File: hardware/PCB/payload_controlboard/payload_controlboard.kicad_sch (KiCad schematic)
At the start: 1 part

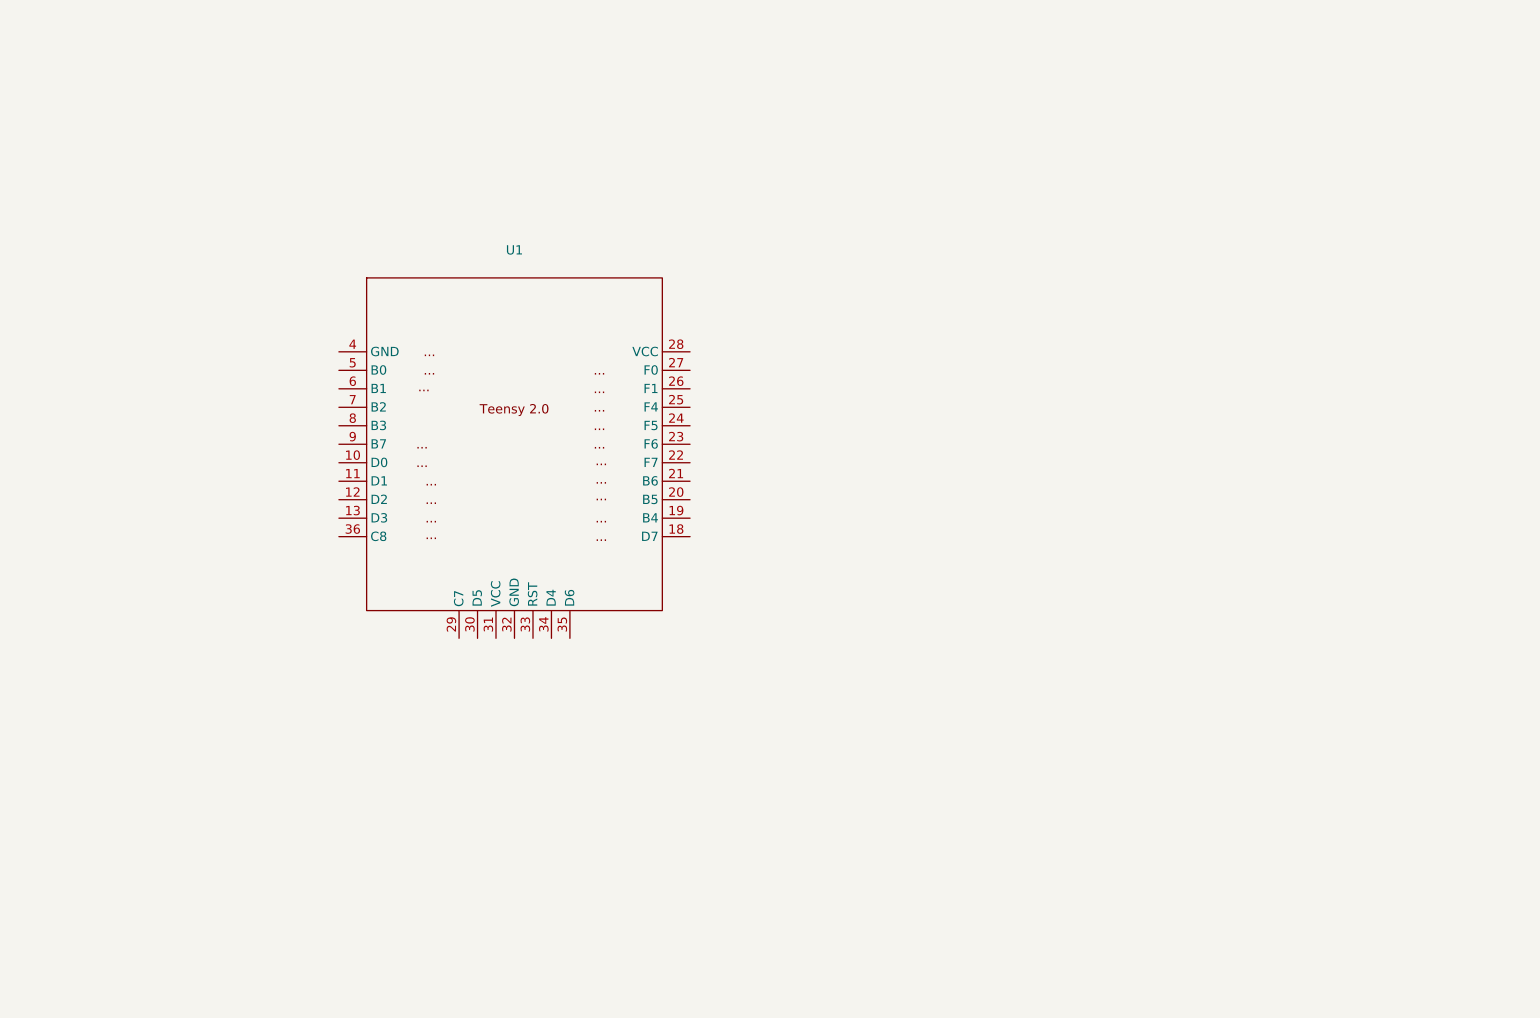
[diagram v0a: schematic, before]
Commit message: Initial payload control board and connector layout
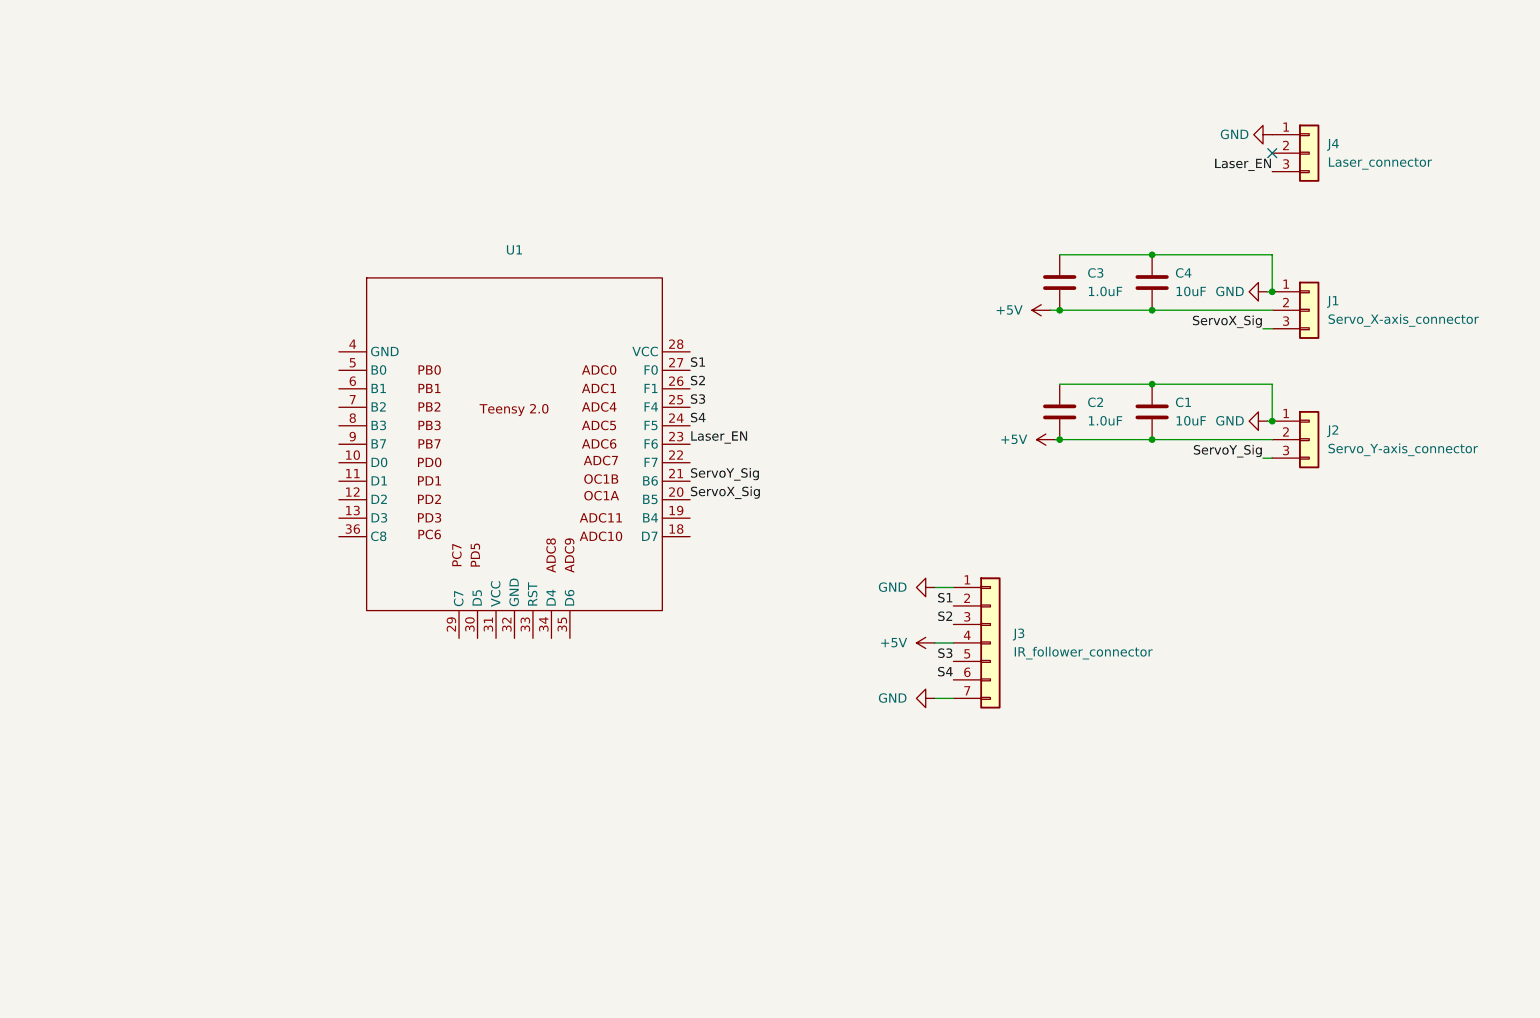
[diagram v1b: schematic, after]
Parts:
- added C1, C4: 10uF, symbol Device:C
- added C2, C3: 1.0uF, symbol Device:C
- added J1: Servo_X-axis_connector, symbol Connector_Generic:Conn_01x03
- added J2: Servo_Y-axis_connector, symbol Connector_Generic:Conn_01x03
- added J3: IR_follower_connector, symbol Connector_Generic:Conn_01x07
- added J4: Laser_connector, symbol Connector_Generic:Conn_01x03
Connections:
- net ServoX_Sig: now reaches U1.20 (B5)
- net ServoX_Sig: now also J1.3 (Pin_3)
- net ServoY_Sig: now reaches U1.21 (B6)
- net ServoY_Sig: now also J2.3 (Pin_3)
- net Laser_EN: now reaches U1.23 (F6)
- net Laser_EN: now also J4.3 (Pin_3)
- net S4: now reaches U1.24 (F5)
- net S4: now also J3.6 (Pin_6)
- net S3: now reaches U1.25 (F4)
- net S3: now also J3.5 (Pin_5)
- net S2: now reaches U1.26 (F1)
- net S2: now also J3.3 (Pin_3)
- net S1: now reaches U1.27 (F0)
- net S1: now also J3.2 (Pin_2)
- new net +5V: C1.2, C2.2, C3.2, C4.2, J1.2 (Pin_2), J2.2 (Pin_2), J3.4 (Pin_4)
- new net GND: C1.1, C2.1, C3.1, C4.1, J1.1 (Pin_1), J2.1 (Pin_1), J3.1 (Pin_1), J3.7 (Pin_7), J4.1 (Pin_1)
- no-connect marks 0 -> 1

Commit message: Added payload connectors and follower->payload compliant connector
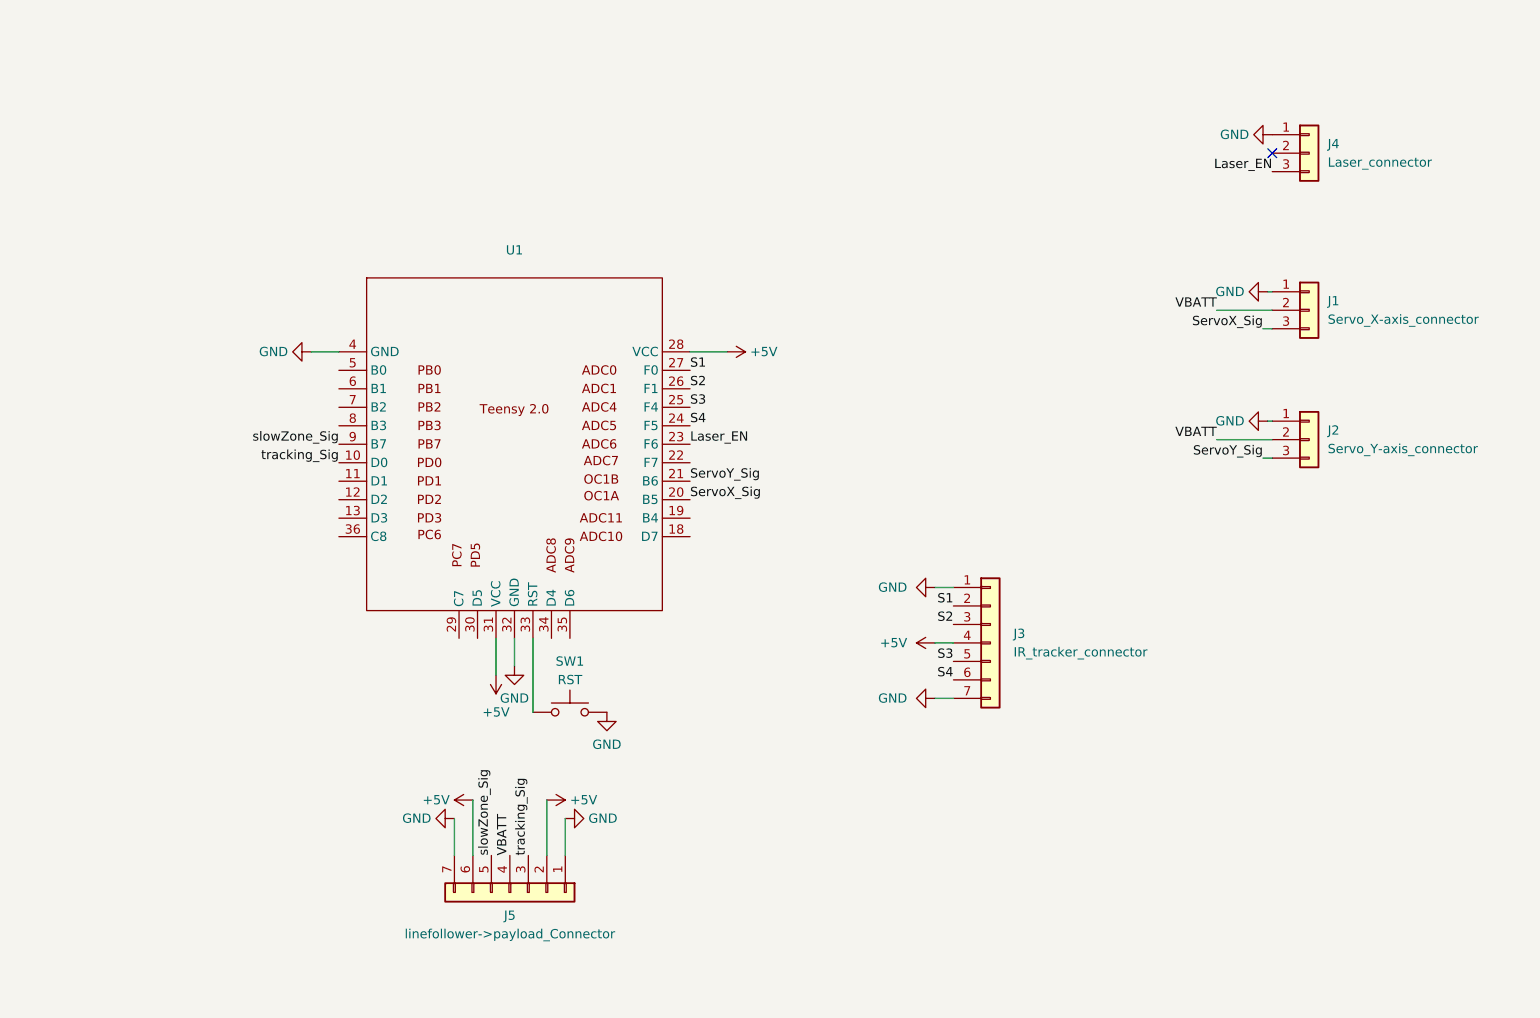
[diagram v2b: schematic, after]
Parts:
- removed C1, C4: 10uF, symbol Device:C
- removed C2, C3: 1.0uF, symbol Device:C
- added J5: linefollower->payload_Connector, symbol Connector_Generic:Conn_01x07
- added SW1: RST, symbol Switch:SW_Push
- J3: value IR_follower_connector -> IR_tracker_connector
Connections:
- net +5V: now also U1.28 (VCC), U1.31 (VCC), J5.2 (Pin_2), J5.6 (Pin_6); no longer J1.2 (Pin_2), J2.2 (Pin_2)
- net GND: now also U1.32 (GND), U1.4 (GND), J5.1 (Pin_1), J5.7 (Pin_7), SW1.2
- net tracking_Sig: now reaches U1.10 (D0)
- net tracking_Sig: now also J5.3 (Pin_3)
- net at U1.33 (RST): now also SW1.1
- net slowZone_Sig: now reaches U1.9 (B7)
- net slowZone_Sig: now also J5.5 (Pin_5)
- new net VBATT: J1.2 (Pin_2), J2.2 (Pin_2), J5.4 (Pin_4)

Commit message: Finished PCBs for payload and turret
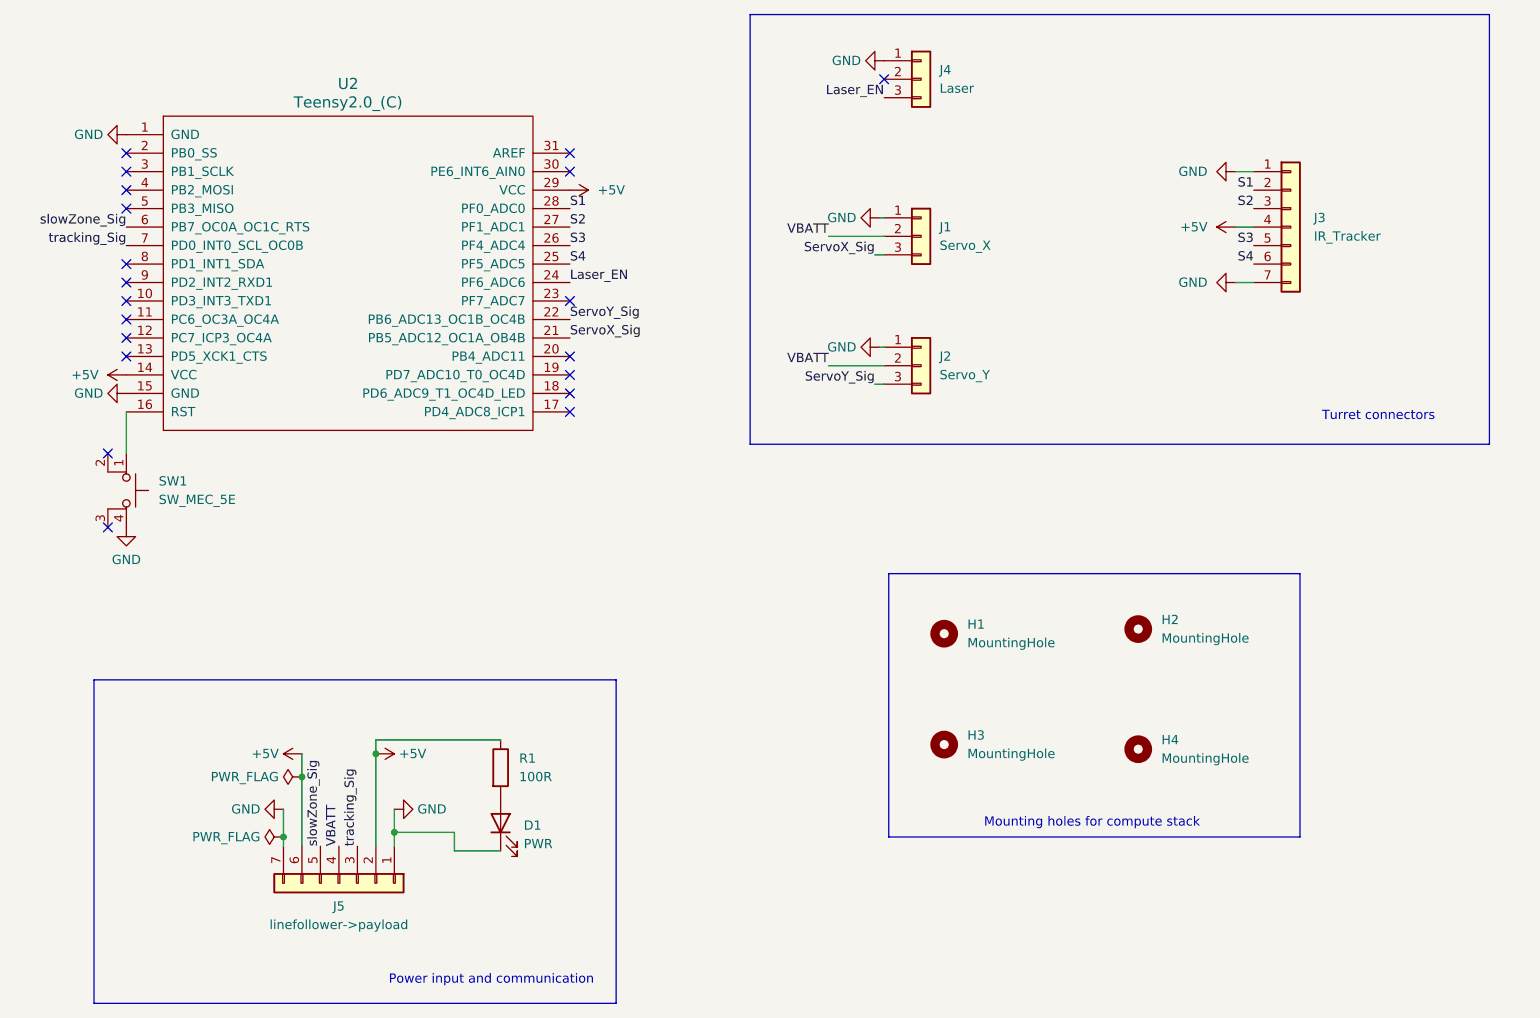
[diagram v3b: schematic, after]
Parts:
- removed SW1: RST, symbol Switch:SW_Push
- removed U1: ~, symbol MCU_Microchip_ATmega:Teensy2.0
- added D1: PWR, LED_THT:LED_D5.0mm, symbol Device:LED
- added H1, H2, H3, H4: MountingHole, MountingHole:MountingHole_3.2mm_M3, symbol Mechanical:MountingHole
- added R1: 100R, Resistor_THT:R_Axial_DIN0207_L6.3mm_D2.5mm_P10.16mm_Horizontal, symbol Device:R
- added SW1: SW_MEC_5E, Button_Switch_THT:SO4_222A-M-V-B_CTS, symbol Switch:SW_MEC_5E
- added U2: Teensy2.0_(C), Module:Teensy2.0, symbol teensy:Teensy2.0_(C)
- J1: value Servo_X-axis_connector -> Servo_X; footprint (none) -> Connector_PinHeader_2.54mm:PinHeader_1x03_P2.54mm_Vertical
- J2: value Servo_Y-axis_connector -> Servo_Y; footprint (none) -> Connector_PinHeader_2.54mm:PinHeader_1x03_P2.54mm_Vertical
- J3: value IR_tracker_connector -> IR_Tracker; footprint (none) -> Connector_PinHeader_2.54mm:PinHeader_1x07_P2.54mm_Vertical
- J4: value Laser_connector -> Laser; footprint (none) -> Connector_PinHeader_2.54mm:PinHeader_1x03_P2.54mm_Vertical
- J5: value linefollower->payload_Connector -> linefollower->payload; footprint (none) -> Connector_PinHeader_2.54mm:PinHeader_1x07_P2.54mm_Vertical
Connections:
- net +5V: now also R1.1, U2.14 (VCC), U2.29 (VCC)
- net GND: now also D1.1 (K), SW1.4 (A), U2.1 (GND), U2.15 (GND)
- net Laser_EN: now also U2.24 (PF6_ADC6)
- net S1: now also U2.28 (PF0_ADC0)
- net S2: now also U2.27 (PF1_ADC1)
- net S3: now also U2.26 (PF4_ADC4)
- net S4: now also U2.25 (PF5_ADC5)
- net ServoX_Sig: now also U2.21 (PB5_ADC12_OC1A_OB4B)
- net ServoY_Sig: now also U2.22 (PB6_ADC13_OC1B_OC4B)
- net slowZone_Sig: now also U2.6 (PB7_OC0A_OC1C_RTS)
- net tracking_Sig: now also U2.7 (PD0_INT0_SCL_OC0B)
- new net: D1.2 (A), R1.2
- new net: SW1.1, U2.16 (RST)
- no-connect marks 1 -> 20
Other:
- note added: "Mounting holes for compute stack"
- note added: "Power input and communication"
- note added: "Turret connectors"
- moved on the sheet: J1, J2, J3, J4, J5

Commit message: payload v2
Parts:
- added SW2: MODE, footprints:SO4_222A-M-V-B_CTS, symbol Switch:SW_MEC_5E
- SW1: value SW_MEC_5E -> RST; footprint Button_Switch_THT:SO4_222A-M-V-B_CTS -> footprints:SO4_222A-M-V-B_CTS
- U2: footprint Module:Teensy2.0 -> footprints:Teensy2.0
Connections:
- net GND: now also SW1.1, SW1.2, SW2.3 (K), SW2.4 (A); no longer SW1.4 (A)
- net at U2.16 (RST): now also SW1.3 (K), SW1.4 (A); no longer SW1.1
- net at U2.17 (PD4_ADC8_ICP1): now also SW2.1, SW2.2
- no-connect marks 20 -> 17
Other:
- company: (none) -> Designed by Maurice Blake
- title: (none) -> Payload control board
- moved on the sheet: SW1
